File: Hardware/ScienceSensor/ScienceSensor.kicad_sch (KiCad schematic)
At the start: 16 parts

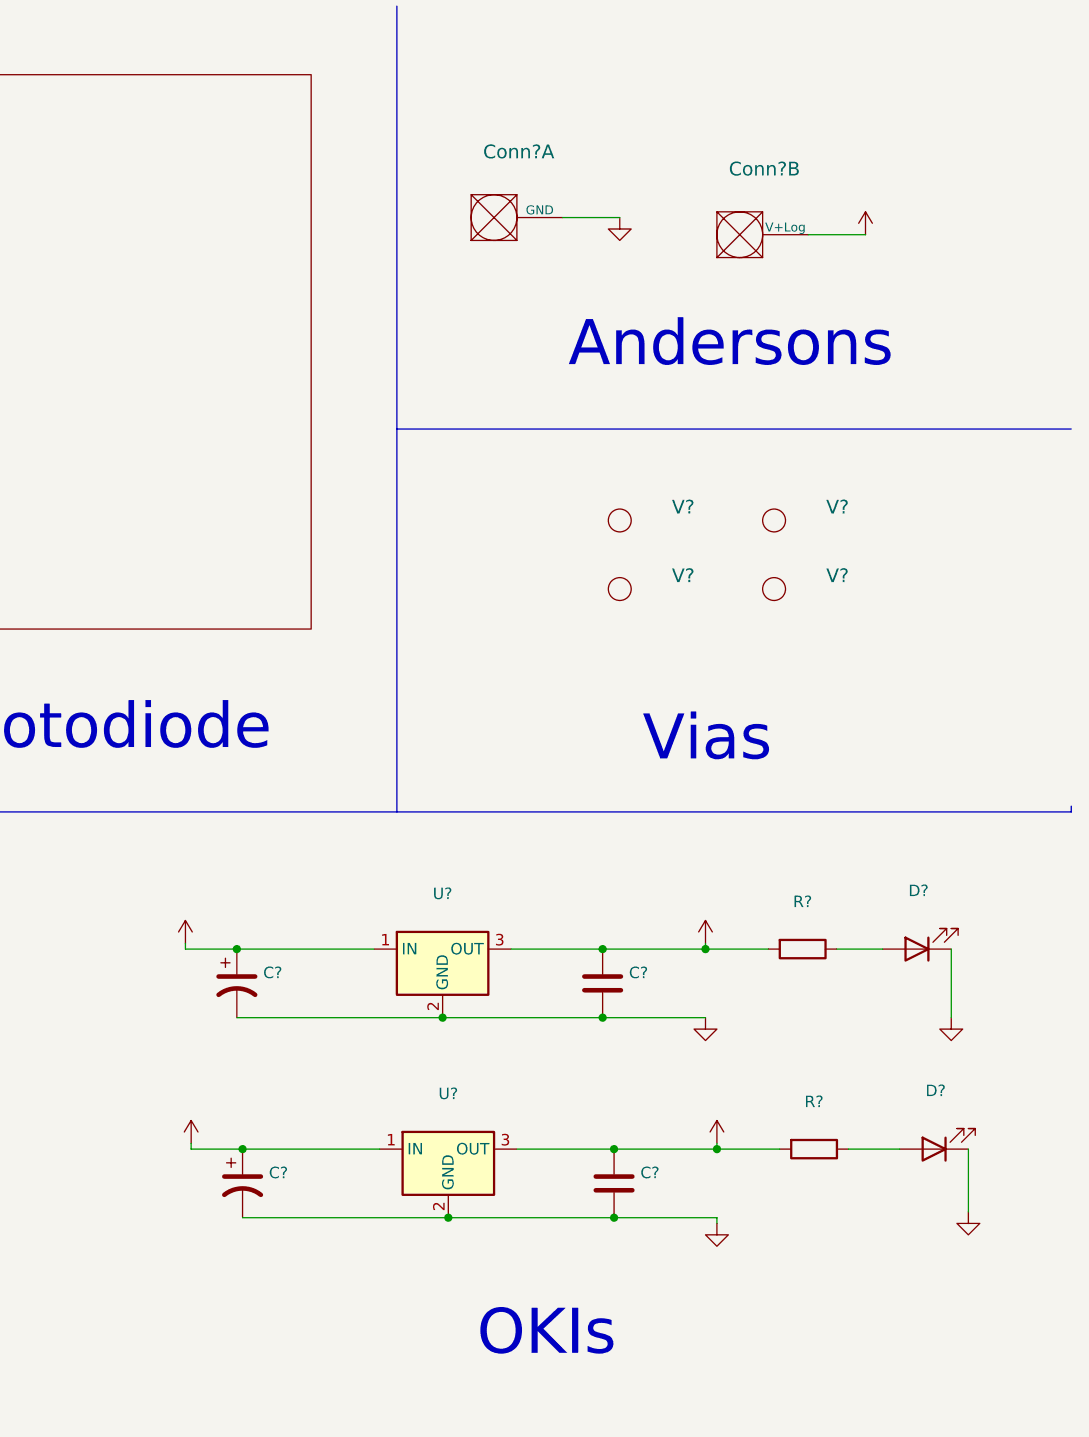
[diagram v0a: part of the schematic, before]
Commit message: Created NO sensor, NH3 sensor, worked on Mosfets, and created Methane sensor with labels.
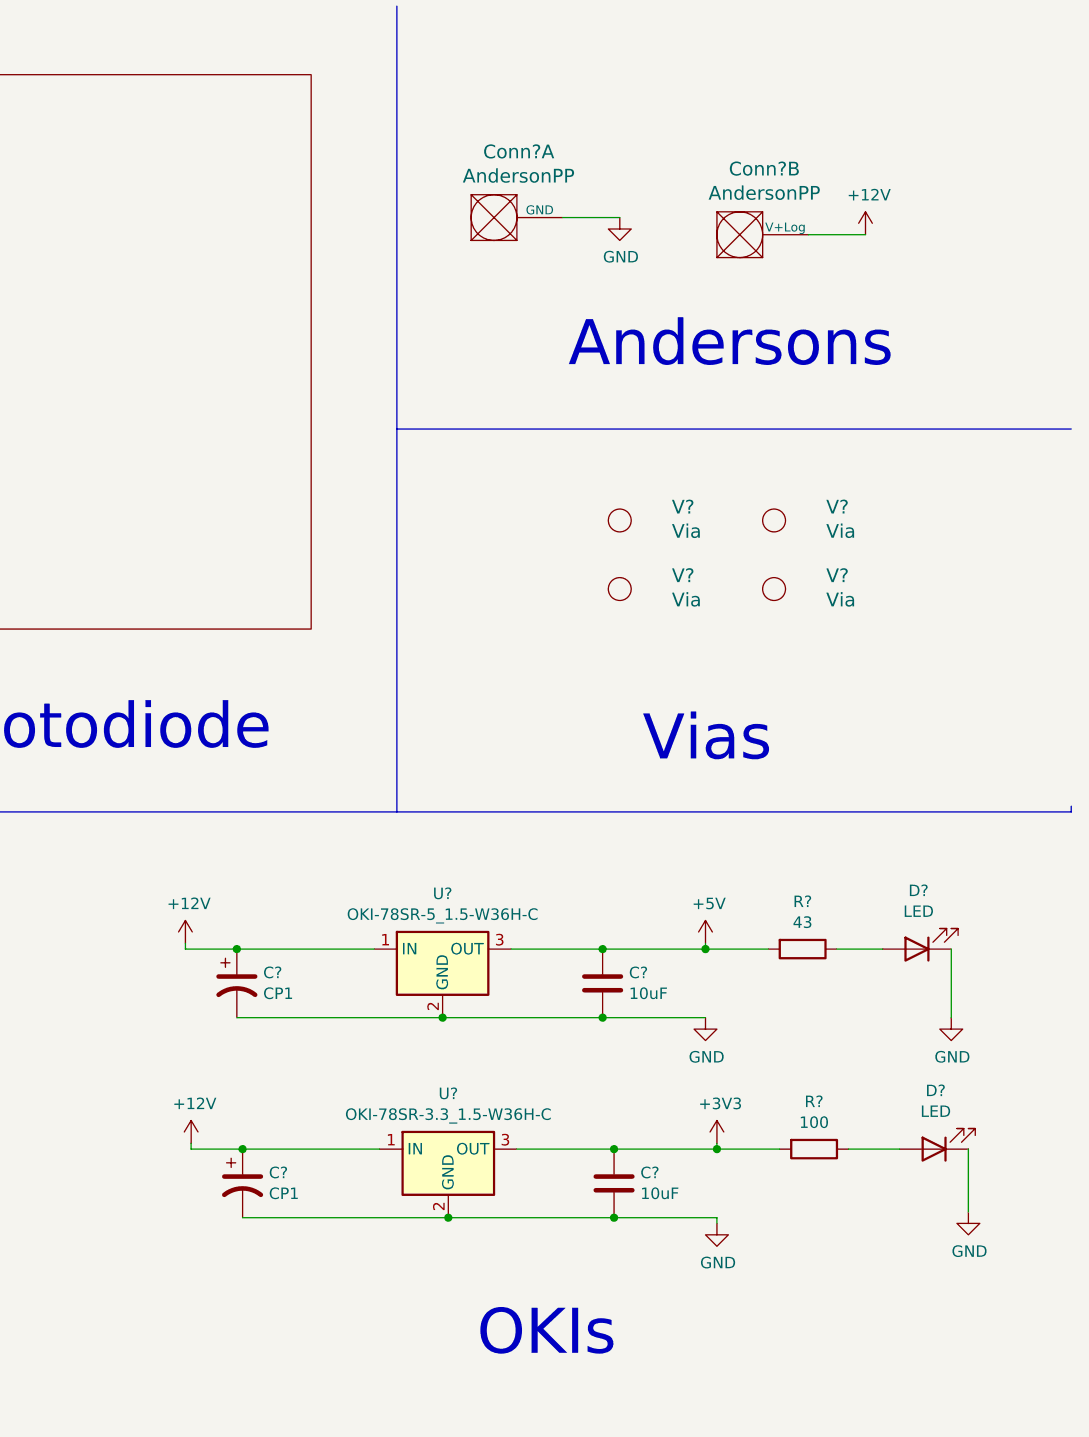
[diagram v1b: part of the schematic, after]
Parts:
- C? (x2): value (none) -> 10uF
- C? (x2): value (none) -> CP1
- Conn? (x2): value (none) -> AndersonPP
- D? (x2): value (none) -> LED
- R?: value (none) -> 43
- R?: value (none) -> 100
- U?: value (none) -> OKI-78SR-5_1.5-W36H-C; footprint (none) -> Converter_DCDC:Converter_DCDC_muRata_OKI-78SR_Horizontal
- U?: value (none) -> OKI-78SR-3.3_1.5-W36H-C; footprint (none) -> Converter_DCDC:Converter_DCDC_muRata_OKI-78SR_Horizontal
- V? (x4): value (none) -> Via

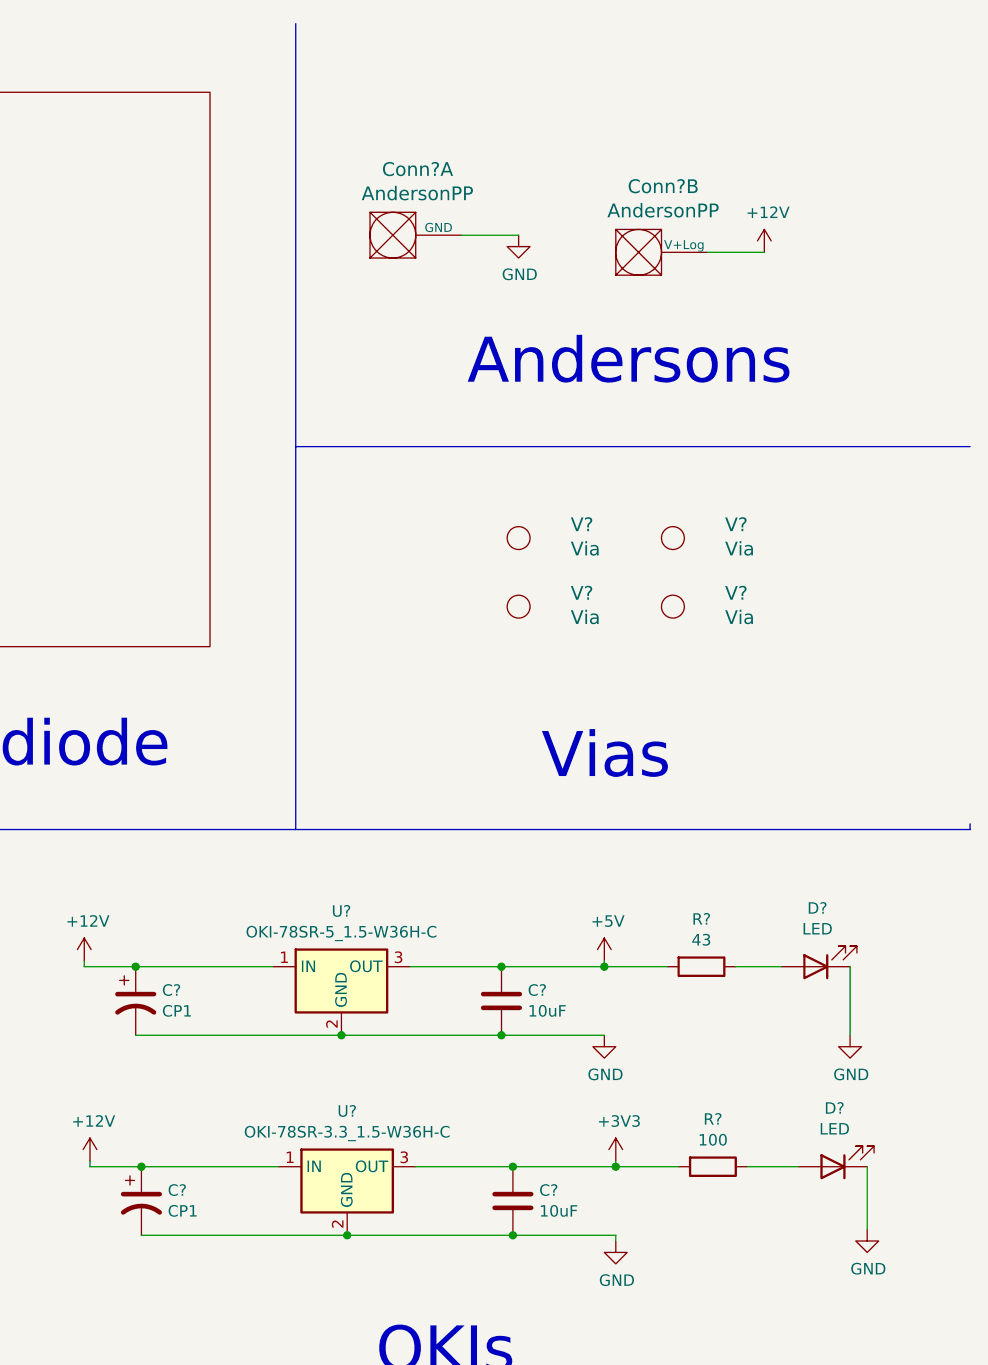
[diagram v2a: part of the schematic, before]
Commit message: BOM generated, photodiodes added
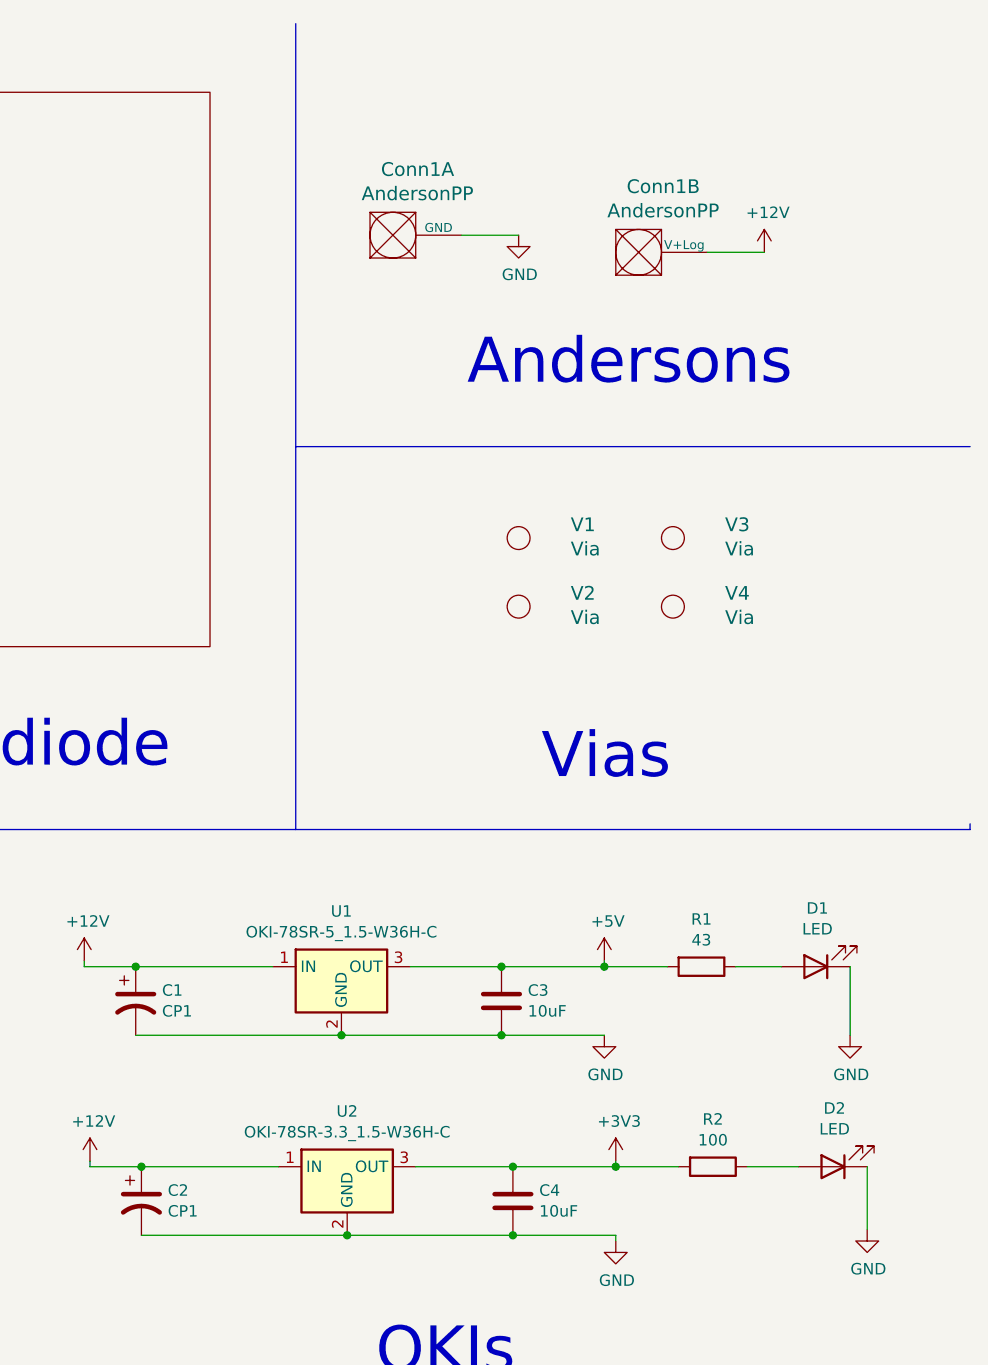
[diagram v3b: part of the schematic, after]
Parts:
- gave numbers to parts that had none: 15

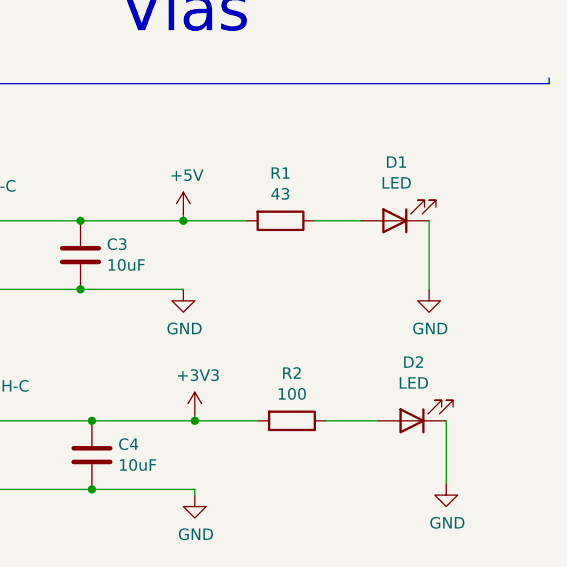
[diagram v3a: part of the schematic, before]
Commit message: Fixed diode ref / values
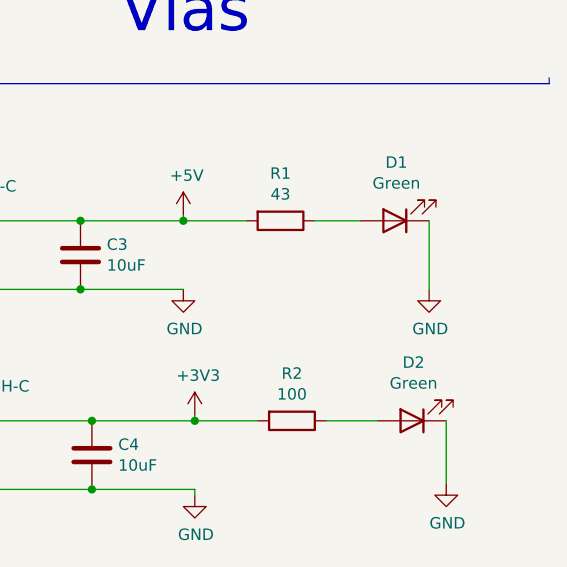
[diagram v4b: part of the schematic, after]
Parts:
- D1, D2: value LED -> Green
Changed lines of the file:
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@@
     (in_bom yes) (on_board yes)
     (property "Reference" "D1" (id 0) (at 267.5128 110.998 0))
-    (property "Value" "LED" (id 1) (at 267.5128 113.3094 0))
+    (property "Value" "Green" (id 1) (at 267.5128 113.3094 0))
     (property "Footprint" "" (id 2) (at 267.335 117.475 0)
       (effects (font (size 1.27 1.27)) hide)
@@
     (in_bom yes) (on_board yes)
     (property "Reference" "D2" (id 0) (at 269.4178 133.223 0))
-    (property "Value" "LED" (id 1) (at 269.4178 135.5344 0))
+    (property "Value" "Green" (id 1) (at 269.4178 135.5344 0))
     (property "Footprint" "" (id 2) (at 269.24 139.7 0)
       (effects (font (size 1.27 1.27)) hide)
@@
       (reference "#PWR052") (unit 1) (value "GND") (footprint "")
     )
+    (path "/00000000-0000-0000-0000-000063213561/2d151e64-47a6-40b0-9adf-3b329b678a8d"
+      (reference "#PWR053") (unit 1) (value "GND") (footprint "")
+    )
+    (path "/00000000-0000-0000-0000-000063213561/89c6678a-66b9-4930-8779-2aca40e943ae"
+      (reference "#PWR054") (unit 1) (value "GND") (footprint "")
+    )
+    (path "/00000000-0000-0000-0000-000063213561/963e5a84-e57e-4dff-bb7c-e7ac238fb98b"
+      (reference "#PWR055") (unit 1) (value "GND") (footprint "")
+    )
     (path "/00000000-0000-0000-0000-000063213561/1a1f6138-ccb4-4597-8f52-82eee96dbf32"
-      (reference "#PWR?") (unit 1) (value "+3.3V") (footprint "")
+      (reference "#PWR056") (unit 1) (value "+3.3V") (footprint "")
+    )
+    (path "/00000000-0000-0000-0000-000063213561/fd7b3858-2983-4f71-b573-f98e4c8dad46"
+      (reference "#PWR057") (unit 1) (value "+3.3V") (footprint "")
     )
     (path "/00000000-0000-0000-0000-000063213561/1c902a6a-fdf6-4214-828e-4663ee8417e2"
-      (reference "#PWR?") (unit 1) (value "+3.3V") (footprint "")
-    )
-    (path "/00000000-0000-0000-0000-000063213561/2d151e64-47a6-40b0-9adf-3b329b678a8d"
-      (reference "#PWR?") (unit 1) (value "GND") (footprint "")
-    )
-    (path "/00000000-0000-0000-0000-000063213561/89c6678a-66b9-4930-8779-2aca40e943ae"
-      (reference "#PWR?") (unit 1) (value "GND") (footprint "")
-    )
-    (path "/00000000-0000-0000-0000-000063213561/963e5a84-e57e-4dff-bb7c-e7ac238fb98b"
-      (reference "#PWR?") (unit 1) (value "GND") (footprint "")
-    )
-    (path "/00000000-0000-0000-0000-000063213561/fd7b3858-2983-4f71-b573-f98e4c8dad46"
-      (reference "#PWR?") (unit 1) (value "+3.3V") (footprint "")
-    )
-    (path "/00000000-0000-0000-0000-00006320eb63/574e4d80-f51f-487f-90d6-96b3965a0a0f"
-      (reference "Blue1") (unit 1) (value "D8") (footprint "")
-    )
-    (path "/00000000-0000-0000-0000-00006320eb63/055708e7-b867-4c33-a274-2c1a1e8b896e"
-      (reference "Blue2") (unit 1) (value "D9") (footprint "")
-    )
-    (path "/00000000-0000-0000-0000-00006320eb63/3938fb23-ef31-4a05-a747-dec8878ca54e"
-      (reference "Blue3") (unit 1) (value "D6") (footprint "")
-    )
-    (path "/00000000-0000-0000-0000-00006320eb63/e4ad2a0d-e733-46df-a51c-1d30f8804430"
-      (reference "Blue4") (unit 1) (value "D7") (footprint "")
-    )
-    (path "/00000000-0000-0000-0000-00006320eb63/89167e31-242e-4a9b-a8af-18fafb9f7758"
-      (reference "Blue5") (unit 1) (value "D12") (footprint "")
-    )
-    (path "/00000000-0000-0000-0000-00006320eb63/980a80b1-0b2a-4728-a472-8442e3fb67ed"
-      (reference "Blue6") (unit 1) (value "D13") (footprint "")
-    )
-    (path "/00000000-0000-0000-0000-00006320eb63/d53e671a-380f-4d04-b3f2-3eccff375d30"
-      (reference "Blue7") (unit 1) (value "D10") (footprint "")
-    )
-    (path "/00000000-0000-0000-0000-00006320eb63/2fdc56b3-fed7-4e1d-ac1a-08f74647780f"
-      (reference "Blue8") (unit 1) (value "D11") (footprint "")
-    )
-    (path "/00000000-0000-0000-0000-00006320eb63/a9de4269-81cc-4c7e-a5c1-ac043d89f15c"
-      (reference "Blue9") (unit 1) (value "D15") (footprint "")
-    )
-    (path "/00000000-0000-0000-0000-00006320eb63/1debd6aa-7706-4123-bd3e-139e95c1e6e3"
-      (reference "Blue10") (unit 1) (value "D14") (footprint "")
+      (reference "#PWR058") (unit 1) (value "+3.3V") (footprint "")
     )
     (path "/00000000-0000-0000-0000-000063223279"
@@
       (reference "Conn8") (unit 1) (value "Molex_SL_02") (footprint "")
     )
+    (path "/00000000-0000-0000-0000-000063213561/da03ad5e-ccaa-469a-8f65-09130dee88c3"
+      (reference "Conn9") (unit 1) (value "Molex_SL_03") (footprint "")
+    )
+    (path "/00000000-0000-0000-0000-000063213561/89ca0d9a-3106-44d8-8eee-2ea4addcd6f9"
+      (reference "Conn10") (unit 1) (value "Molex_SL_03") (footprint "")
+    )
     (path "/00000000-0000-0000-0000-000063213561/7a8c584b-4135-4470-91e4-82042dfe42ea"
-      (reference "Conn?") (unit 1) (value "Molex_SL_03") (footprint "")
-    )
-    (path "/00000000-0000-0000-0000-000063213561/89ca0d9a-3106-44d8-8eee-2ea4addcd6f9"
-      (reference "Conn?") (unit 1) (value "Molex_SL_03") (footprint "")
-    )
-    (path "/00000000-0000-0000-0000-000063213561/da03ad5e-ccaa-469a-8f65-09130dee88c3"
-      (reference "Conn?") (unit 1) (value "Molex_SL_03") (footprint "")
+      (reference "Conn11") (unit 1) (value "Molex_SL_03") (footprint "")
     )
     (path "/00000000-0000-0000-0000-000063231caf"
-      (reference "D1") (unit 1) (value "LED") (footprint "")
+      (reference "D1") (unit 1) (value "Green") (footprint "")
     )
     (path "/00000000-0000-0000-0000-0000632324b5"
-      (reference "D2") (unit 1) (value "LED") (footprint "")
+      (reference "D2") (unit 1) (value "Green") (footprint "")
     )
     (path "/00000000-0000-0000-0000-00006320ec71/00000000-0000-0000-0000-0000632159fd"
@@
     )
     (path "/00000000-0000-0000-0000-000063213561/00000000-0000-0000-0000-000063267298"
-      (reference "D6") (unit 1) (value "LED") (footprint "")
+      (reference "D6") (unit 1) (value "Blue") (footprint "")
     )
     (path "/00000000-0000-0000-0000-000063213561/00000000-0000-0000-0000-000063270eb8"
-      (reference "D7") (unit 1) (value "LED") (footprint "")
+      (reference "D7") (unit 1) (value "Blue") (footprint "")
     )
     (path "/00000000-0000-0000-0000-000063213561/00000000-0000-0000-0000-000063255ac6"
-      (reference "D8") (unit 1) (value "LED") (footprint "")
+      (reference "D8") (unit 1) (value "Blue") (footprint "")
+    )
+    (path "/00000000-0000-0000-0000-00006320eb63/574e4d80-f51f-487f-90d6-96b3965a0a0f"
+      (reference "D9") (unit 1) (value "Blue") (footprint "")
+    )
+    (path "/00000000-0000-0000-0000-00006320eb63/055708e7-b867-4c33-a274-2c1a1e8b896e"
+      (reference "D10") (unit 1) (value "Blue") (footprint "")
+    )
+    (path "/00000000-0000-0000-0000-00006320eb63/3938fb23-ef31-4a05-a747-dec8878ca54e"
+      (reference "D11") (unit 1) (value "Blue") (footprint "")
+    )
+    (path "/00000000-0000-0000-0000-00006320eb63/e4ad2a0d-e733-46df-a51c-1d30f8804430"
+      (reference "D12") (unit 1) (value "Blue") (footprint "")
+    )
+    (path "/00000000-0000-0000-0000-00006320eb63/89167e31-242e-4a9b-a8af-18fafb9f7758"
+      (reference "D13") (unit 1) (value "Blue") (footprint "")
+    )
+    (path "/00000000-0000-0000-0000-00006320eb63/980a80b1-0b2a-4728-a472-8442e3fb67ed"
+      (reference "D14") (unit 1) (value "Blue") (footprint "")
+    )
+    (path "/00000000-0000-0000-0000-00006320eb63/d53e671a-380f-4d04-b3f2-3eccff375d30"
+      (reference "D15") (unit 1) (value "Blue") (footprint "")
+    )
+    (path "/00000000-0000-0000-0000-00006320eb63/2fdc56b3-fed7-4e1d-ac1a-08f74647780f"
+      (reference "D16") (unit 1) (value "Blue") (footprint "")
+    )
+    (path "/00000000-0000-0000-0000-00006320eb63/a9de4269-81cc-4c7e-a5c1-ac043d89f15c"
+      (reference "D17") (unit 1) (value "Blue") (footprint "")
+    )
+    (path "/00000000-0000-0000-0000-00006320eb63/1debd6aa-7706-4123-bd3e-139e95c1e6e3"
+      (reference "D18") (unit 1) (value "Blue") (footprint "")
     )
     (path "/00000000-0000-0000-0000-00006320eb63/4019743e-abfb-4451-82ef-f7a09e940ac4"
@@
     )
     (path "/00000000-0000-0000-0000-000063213561/00000000-0000-0000-0000-000063267292"
-      (reference "R14") (unit 1) (value "1k") (footprint "")
+      (reference "R14") (unit 1) (value "100") (footprint "")
     )
     (path "/00000000-0000-0000-0000-00006320eb63/1095357d-74c0-46f0-976e-415d08d1b80f"
@@
     )
     (path "/00000000-0000-0000-0000-000063213561/00000000-0000-0000-0000-000063270eb2"
-      (reference "R16") (unit 1) (value "1k") (footprint "")
+      (reference "R16") (unit 1) (value "100") (footprint "")
     )
     (path "/00000000-0000-0000-0000-000063213561/00000000-0000-0000-0000-000063254d86"
-      (reference "R17") (unit 1) (value "1k") (footprint "")
+      (reference "R17") (unit 1) (value "100") (footprint "")
     )
     (path "/00000000-0000-0000-0000-00006320eb63/43e149dc-082c-4a6f-900f-eb6885ea1a46"
